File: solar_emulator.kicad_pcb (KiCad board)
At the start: 2 copper layers, 95 x 73 mm, 80 parts, among them J1 USB_C_Receptacle_USB2.0_16P, J2 Conn_01x02, J3 Conn_01x02, J4 Conn_01x02, J5 Conn_01x02, J6 Conn_01x03, J7 Conn_01x04, Q1 IRFZ44N, Q2 IRFZ44N, Q3 IRFZ44N, Q4 IRFZ44N, Q5 IRFZ44N, Q6 IRFZ44N, Q7 IRFZ44N, Q8 IRFZ44N, SW1 SW_Push, SW2 SW_Push, U1 ESP32-S3-WROOM-1, U2 LD1117S33TR_SOT223, U3 HIP4081AIPZ, U4 HIP4081AIPZ, U5 LM393, U6 LM393, U7 USBLC6-2SC6

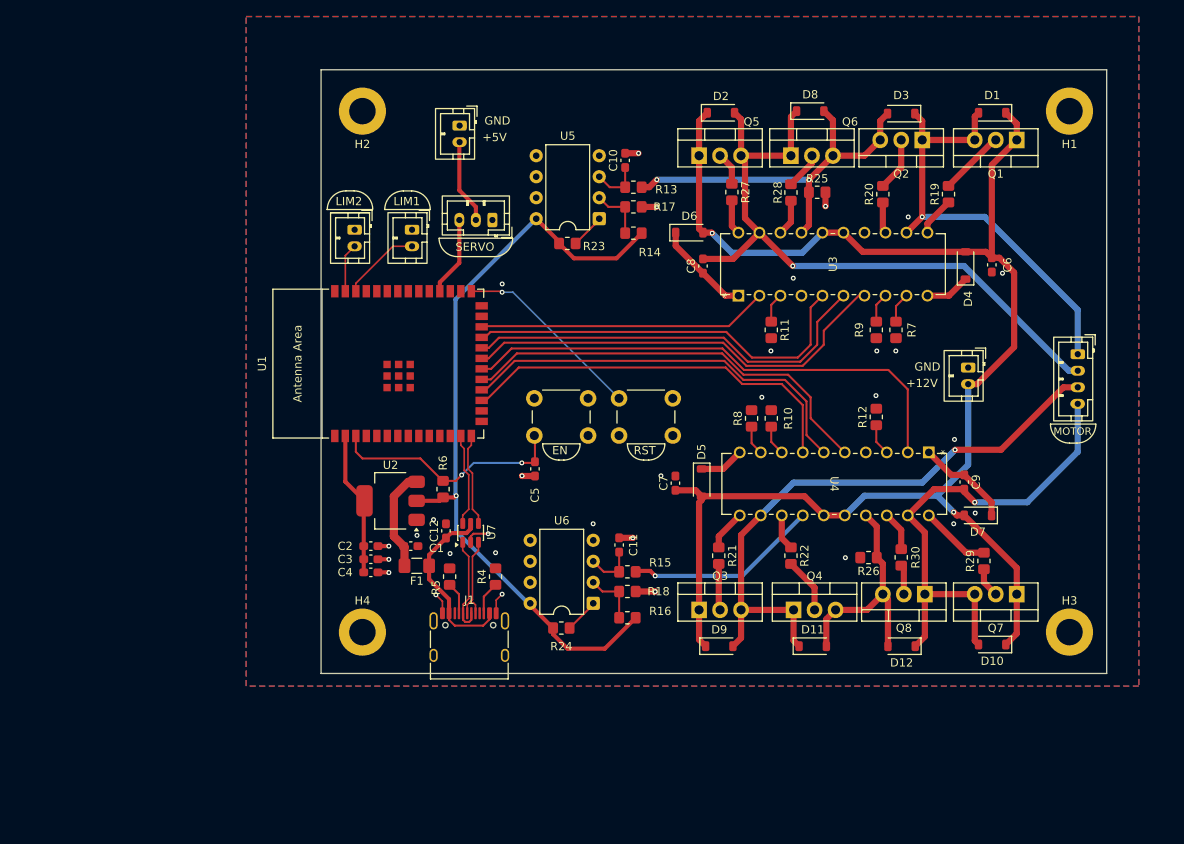
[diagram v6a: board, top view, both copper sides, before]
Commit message: rearrange connectors, traces, add via stitching
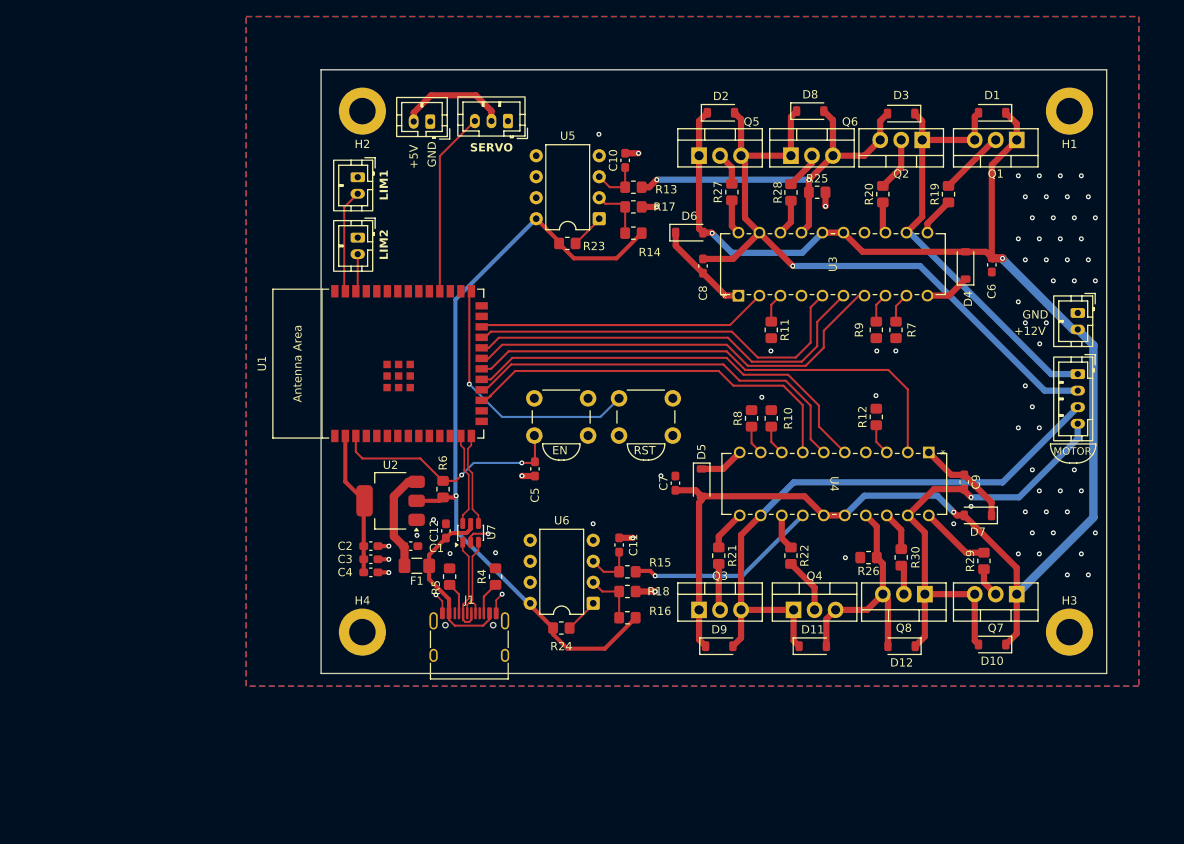
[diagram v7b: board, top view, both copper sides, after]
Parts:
- moved J3 14.8 mm to (235.5, 91.4)
- moved J6 12.1 mm to (166.6, 68.2)
- moved J2 9.14 mm to (148.4, 75.0)
- moved J4 3.58 mm to (157.2, 68.3), turned to 180 degrees
- moved J7 2.41 mm to (235.5, 98.8)
- moved J5 1.03 mm to (148.4, 82.3)
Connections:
- U1 pad 38: LIMIT1 -> LIMIT2
- U1 pad 39: LIMIT2 -> LIMIT1
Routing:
- net +12V: track 183.1 -> 199.1 mm, vias 2 -> 3
- net SERVO: track 9.59 -> 22.3 mm
- net GPIO0: track 23.2 -> 32.0 mm
- net BHS2: track 61.0 -> 56.6 mm
- net 5V: track 10.4 -> 13.4 mm
- net LIMIT1: track 9.61 -> 12.5 mm
- net LIMIT2: track 5.90 -> 4.58 mm
- net MOTOR1: track 54.2 -> 53.2 mm, vias 1 -> 0
- net MOTOR3: track 73.0 -> 72.0 mm, vias 1 -> 0
- net BHS1: track 81.0 -> 82.0 mm
- net GND: vias 31 -> 74

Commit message: did something
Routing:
- net GND: vias 74 -> 91
